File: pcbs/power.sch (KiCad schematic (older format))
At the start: 15 parts, among them J3 Barrel_Jack, U34 TS30011/12/13

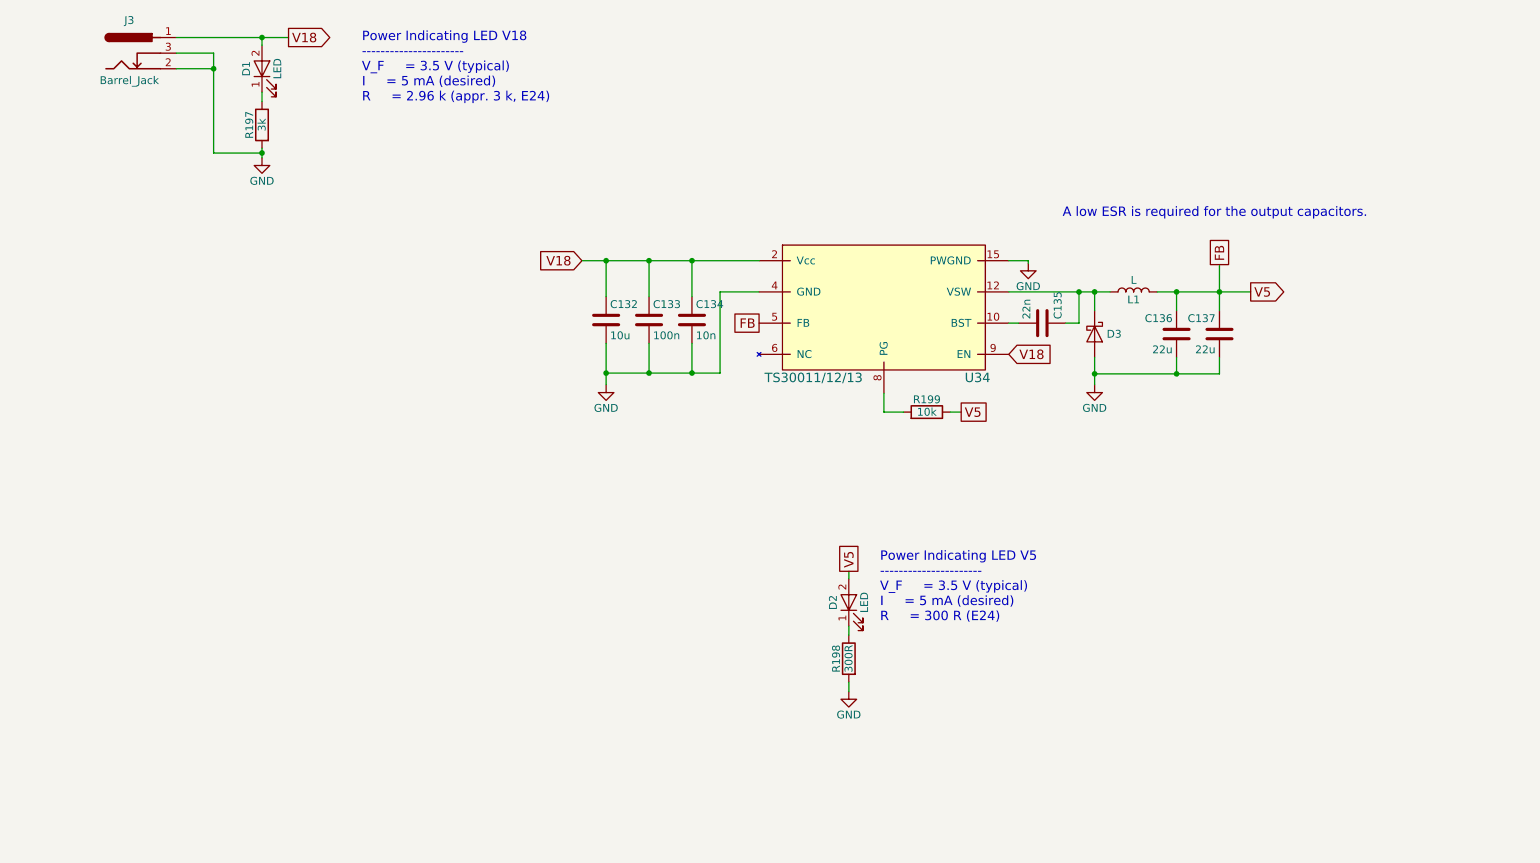
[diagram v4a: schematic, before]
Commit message: No DRC errors anymore in schematics.
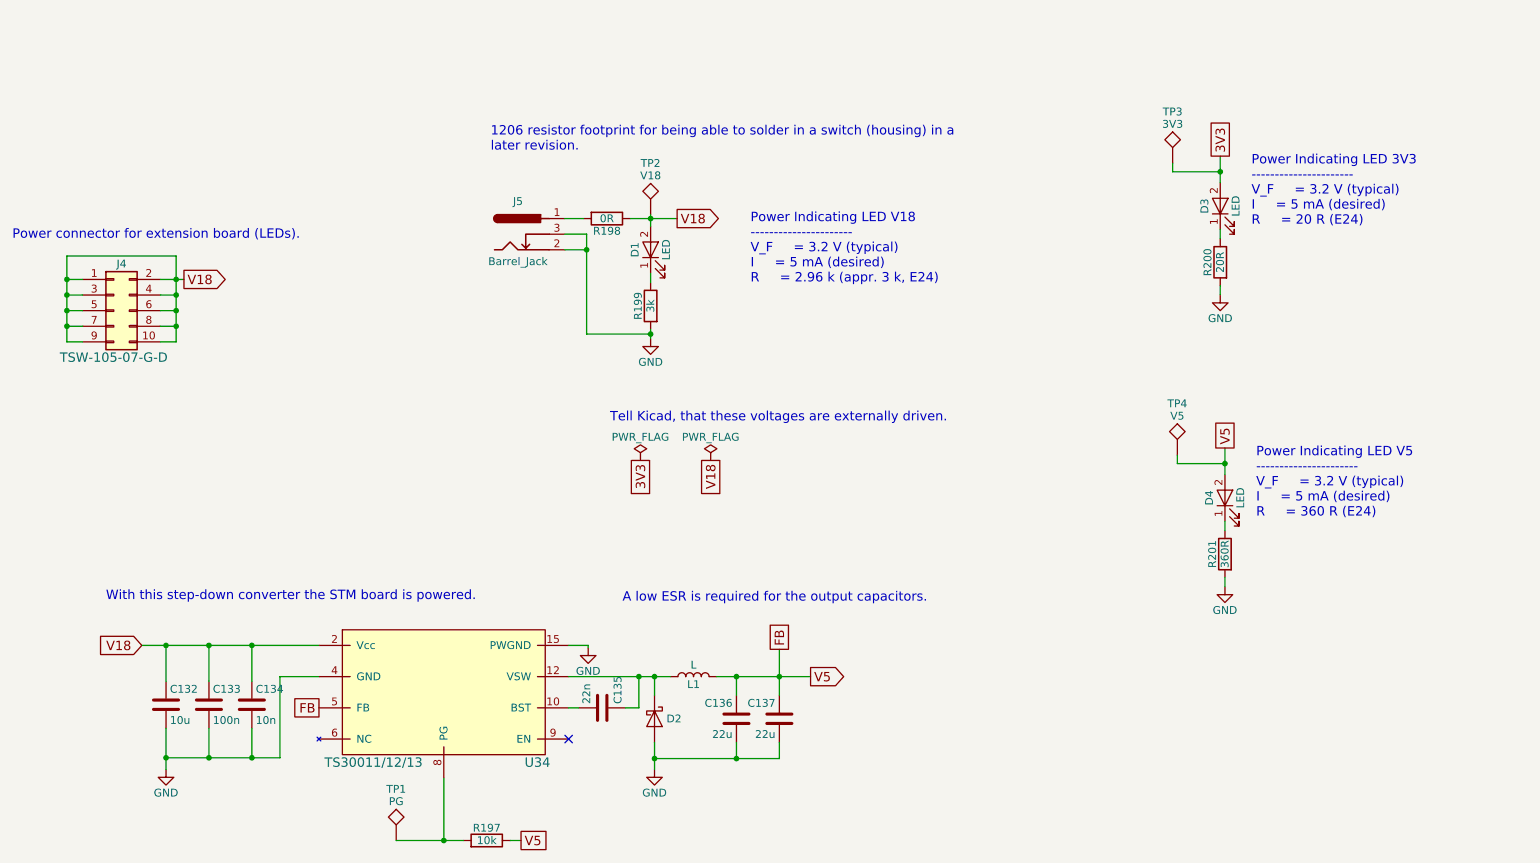
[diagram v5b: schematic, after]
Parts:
- added D3: LED, LEDs:LED_0603, symbol LED
- added J4: Conn_02x05_Odd_Even, Pin_Headers:Pin_Header_Straight_2x05_Pitch2.54mm, symbol Conn_02x05_Odd_Even
- added R198: 0R, Resistors_SMD:R_1206, symbol R
- added R200: 20R, Resistors_SMD:R_0603, symbol R
- added TP1: PG, MyTestpoints:TP_SMD_quadr_1mm, symbol TEST
- added TP2: V18, MyTestpoints:TP_SMD_quadr_1mm, symbol TEST
- added TP3: 3V3, MyTestpoints:TP_SMD_quadr_1mm, symbol TEST
- added TP4: V5, MyTestpoints:TP_SMD_quadr_1mm, symbol TEST
- R201: renamed from R198; value 300R -> 360R; Digikey P300HCT-ND -> 311-360GRCT-ND
- renumbered D3 to D2, D2 to D4, J3 to J5, R199 to R197, R197 to R199
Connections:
- net V5 is gone; now on net FB: C136.1, C137.1, D4.2 (A), L1.2, R197.1
- net FB: now also TP4.1
- net GND: now also R200.2
- net Vcc: now also J4.1 (Pin_1), J4.10 (Pin_10), J4.2 (Pin_2), J4.3 (Pin_3), J4.4 (Pin_4), J4.5 (Pin_5), J4.6 (Pin_6), J4.7 (Pin_7), J4.8 (Pin_8), J4.9 (Pin_9), R198.1, TP2.1; no longer J5.1, U34.9 (EN)
- net at R197.2, U34.8 (PG): now also TP1.1
- new net: J5.1, R198.2
- new net: D3.1 (K), R200.1
- new net 3V3: D3.2 (A), TP3.1
- no-connect marks 0 -> 1
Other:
- note added: "1206 resistor footprint for being able to solder in a switch (housing) in a\nlater revision."
- note added: "Power Indicating LED 3V3\n----------------------\nV_F = 3.2 V (typical)\nI = 5 mA (desired)\nR = 20 R (E24)"
- note added: "Power Indicating LED V18\n----------------------\nV_F = 3.2 V (typical)\nI = 5 mA (desired)\nR = 2.96 k (appr. 3 k, E24)"
- note added: "Power Indicating LED V5\n----------------------\nV_F = 3.2 V (typical)\nI = 5 mA (desired)\nR = 360 R (E24)"
- note added: "Power connector for extension board (LEDs)."
- note added: "Tell Kicad, that these voltages are externally driven."
- note added: "With this step-down converter the STM board is powered."
- note removed: "Power Indicating LED V18\n----------------------\nV_F = 3.5 V (typical)\nI = 5 mA (desired)\nR = 2.96 k (appr. 3 k, E24)"
- note removed: "Power Indicating LED V5\n----------------------\nV_F = 3.5 V (typical)\nI = 5 mA (desired)\nR = 300 R (E24)"
- moved on the sheet: C132, C133, C134, C135, C136, C137, D1, D2, D4, J5, L1, R197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
